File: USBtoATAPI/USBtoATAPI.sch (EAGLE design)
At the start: 3 parts, among them J2 10118192-0002LF

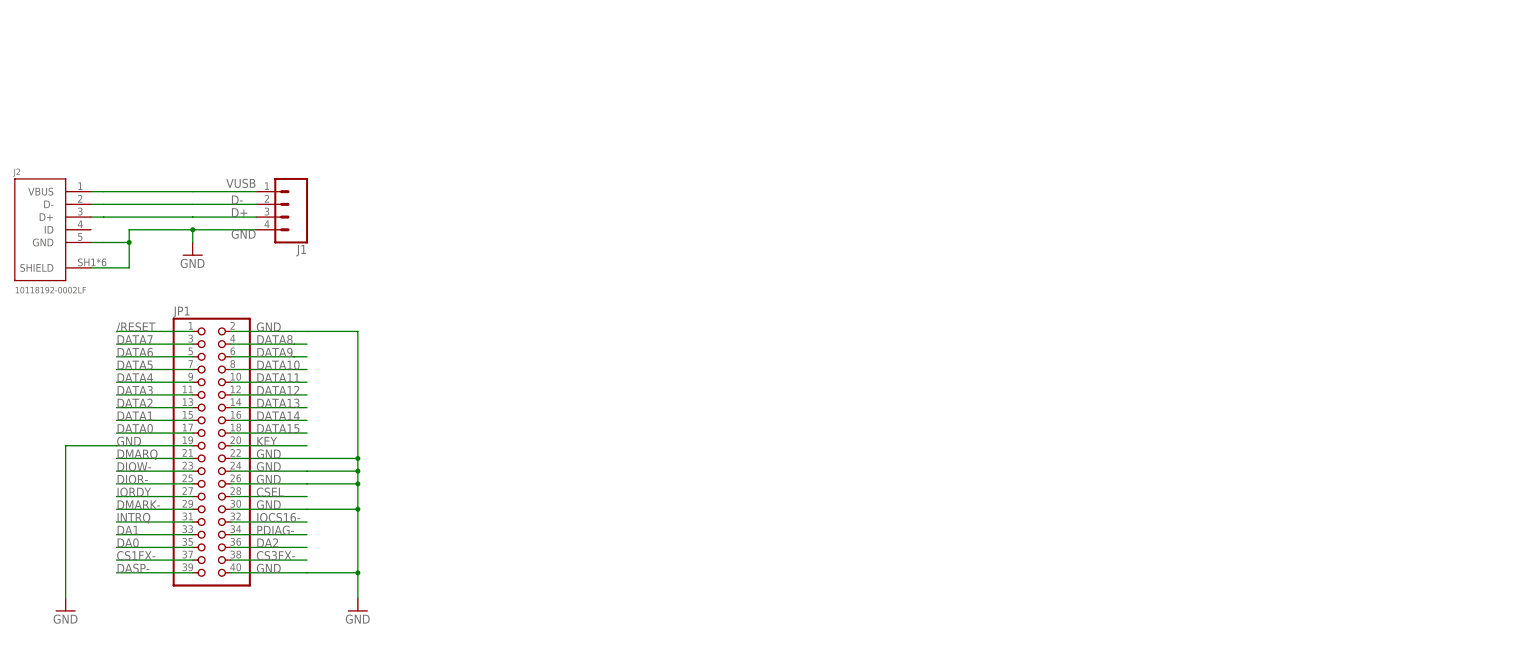
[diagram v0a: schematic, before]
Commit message: Started layout
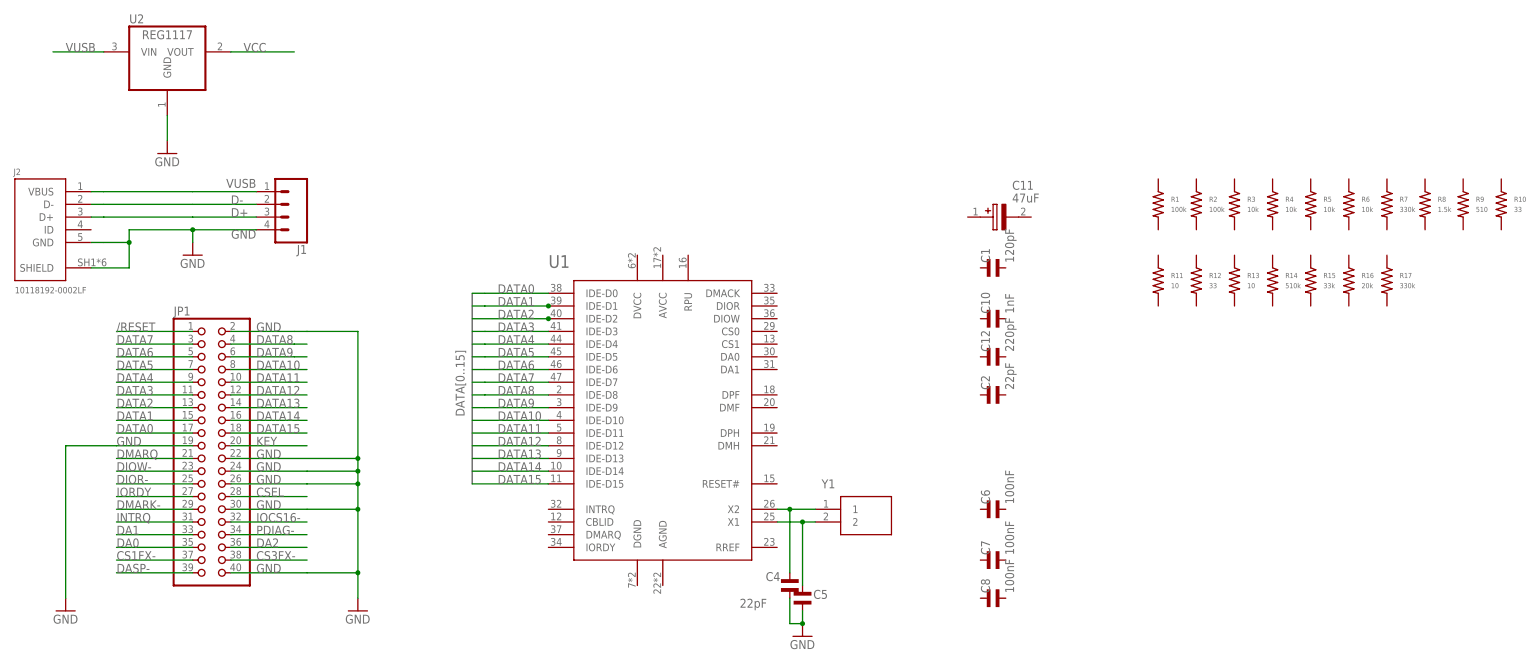
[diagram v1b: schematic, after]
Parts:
- added C1: 120pF, MF_Passives:CAPACITOR_NP_0805
- added C10: 1nF, MF_Passives:CAPACITOR_NP_0805
- added C11: 47uF, SamacSys_Parts:UWR0J470MCL1GB
- added C12: 220pF, MF_Passives:CAPACITOR_NP_0805
- added C2, C4, C5: 22pF, MF_Passives:CAPACITOR_NP_0805
- added C6, C7, C8: 100nF, MF_Passives:CAPACITOR_NP_0805
- added R1, R2: 100k, MF_Passives:RESISTOR_0805
- added R10, R12: 33, MF_Passives:RESISTOR_0805
- added R11, R13: 10, MF_Passives:RESISTOR_0805
- added R14: 510k, MF_Passives:RESISTOR_0805
- added R15: 33k, MF_Passives:RESISTOR_0805
- added R16: 20k, MF_Passives:RESISTOR_0805
- added R17, R7: 330k, MF_Passives:RESISTOR_0805
- added R3, R4, R5, R6: 10k, MF_Passives:RESISTOR_0805
- added R8: 1.5k, MF_Passives:RESISTOR_0805
- added R9: 510, MF_Passives:RESISTOR_0805
- added U1: GL811E, GenesisLogic:GL811E
- added U2: REG1117, burr-brown:REG1117
- added Y1: 445C33C12M00000, SamacSys_Parts:445C33C12M00000
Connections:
- new net N$1: C4.P$1, U1.X2, Y1.1
- new net N$2: C5.P$2, U1.X1, Y1.2
- new net VCC: U2.VOUT
- net DATA0: now also U1.IDE-D0, U1.IDE-D1
- net DATA1: now also U1.IDE-D2
- net DATA10: now also U1.IDE-D10
- net DATA11: now also U1.IDE-D11
- net DATA12: now also U1.IDE-D12
- net DATA13: now also U1.IDE-D13
- net DATA14: now also U1.IDE-D14
- net DATA15: now also U1.IDE-D15
- net DATA3: now also U1.IDE-D3
- net DATA4: now also U1.IDE-D4
- net DATA5: now also U1.IDE-D5
- net DATA6: now also U1.IDE-D6
- net DATA7: now also U1.IDE-D7
- net DATA8: now also U1.IDE-D8
- net DATA9: now also U1.IDE-D9
- net GND: now also C4.P$2, C5.P$1, U2.GND
- net VUSB: now also U2.VIN
